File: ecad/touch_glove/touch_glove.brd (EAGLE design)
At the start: 70.4 x 40.6 mm, 181 parts, among them Q1 MCH3474 4A/30V/50mΩ, Q2 MCH3474 4A/30V/50mΩ, Q3 MCH3474 4A/30V/50mΩ, Q4 MCH3474 4A/30V/50mΩ, Q5 MCH3474 4A/30V/50mΩ, Q6 MCH3474 4A/30V/50mΩ, SW1 4A/28V, Y2 16MHz

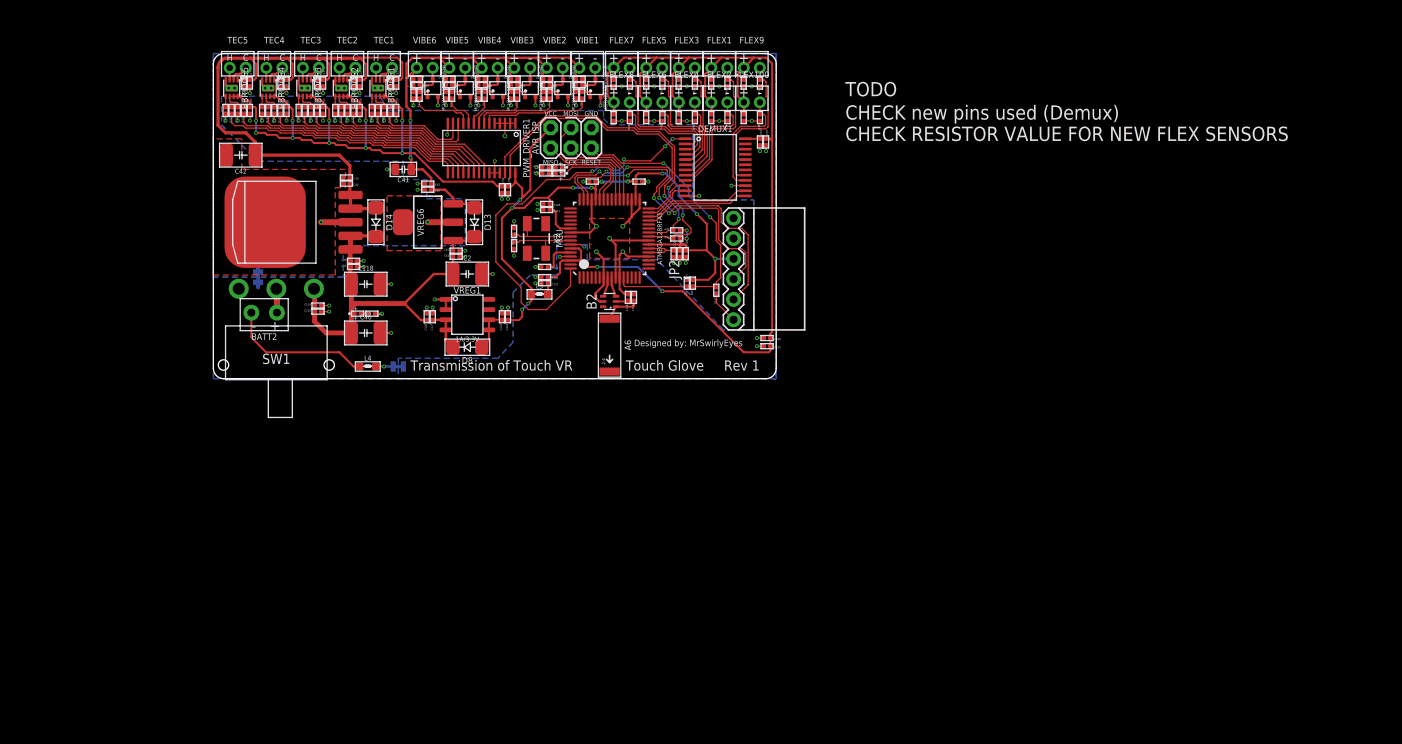
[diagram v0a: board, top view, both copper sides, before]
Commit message: Rev 2: Complete transformation.  Start by replacing parts with new 3D models and new packages.
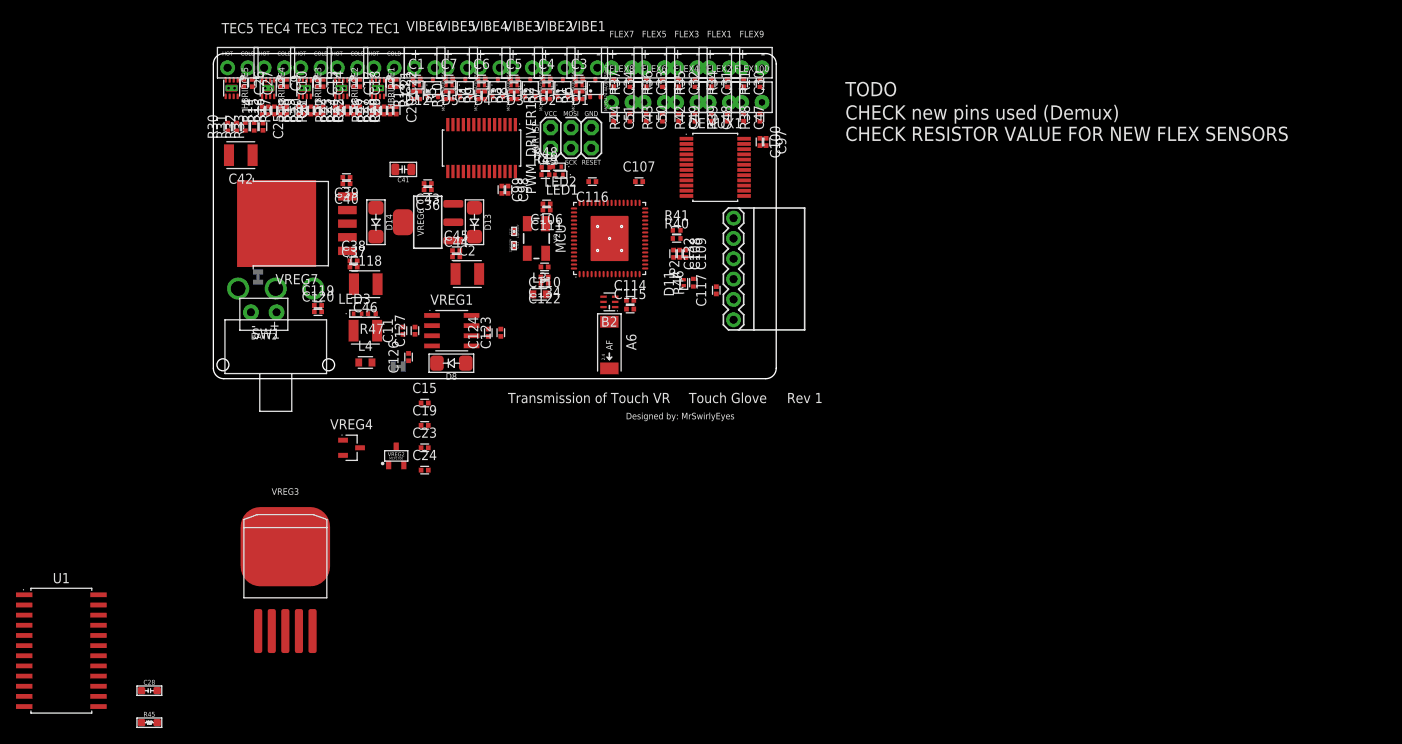
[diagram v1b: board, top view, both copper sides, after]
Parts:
- removed C135: 0.1uF/50V, PiB_capacitors:_CER_SMD_0402
- removed C136: 1uF/25V, PiB_capacitors:_CER_SMD_0402
- added C11, C15, C23: 0.1uF/50V, PiB_capacitors:CAPC1005X55
- added C19, C24: 10uF/6.3V, PiB_capacitors:CAPC1005X55
- added C28: 0.1uF/25V, PiB_capacitors:_CER_SMD-603
- added R45: 1KΩ, PiB_resistors:RESISTOR_SMD-603
- added U1: (no value), PiB:SOIC127P1030X265-24
- added VREG2: 3.3V/250mA, PiB_ic_power:MCP1700_SOT-23
- added VREG3: 5A/5V, PiB_ic_power:TO-263-5
- added VREG4: (no value), PiB_ic_power:SOT95P237X112-3
- A6: value 2.4GHz/802.11/0.5dBi/3W -> 2.45GHz; device PiB_radio_frequency:ANTENNA-CHIP5 -> PiB_radio_frequency:ANTC6522X100
- B2: value Impedence UNBAL/BAL (50Ω/100Ω) -> 50/100; device PiB_radio_frequency:0805_BALUN -> PiB_radio_frequency:RESCAXE65P200X125X95-6
- C1, C100, C106, C107, C108, C109, C110, C111, C115, C116, C117, C119, C12, C122, C124, C127, C13, C132, C134, C16, C17, C20, C21, C25, C26, C3, C30, C31, C32, C33, C34, C36, C38, C4, C40, C45, C47, C48, C49, C5, C50, C51, C6, C7, C8, C9, C98: device PiB_capacitors:_CER_SMD_0402 -> PiB_capacitors:CAPC1005X55
- C10, C120, C123, C126, C14, C18, C22, C27, C37, C39, C43, C44, C97, C99: value 10uF/10V -> 10uF/6.3V; device PiB_capacitors:_CER_SMD_0402 -> PiB_capacitors:CAPC1005X55
- C112, C113: device PiB_capacitors:_CER_SMD_0402 -> PiB_capacitors:_CER_SMD-402
- C114: value 22pF/50V -> 22pF/100V; device PiB_capacitors:_CER_SMD_0402 -> PiB_capacitors:CAPC1005X55
- C118, C2, C42, C46: device PiB_capacitors:_CER_SMD-1210 -> PiB_capacitors:CAPC3225X270
- D1, D11, D12, D2, D3, D4, D5: device PiB_discrete_semiconductors:SOD-923F/0402 -> PiB_discrete_semiconductors:DFN100X60X55-2
- DEMUX1: device PiB:SSOP-24 -> PiB:SOP65P780X200-24
- JP2: value FTDIPTH-RA -> (none)
- L3, L4: value 10uH/0.38A -> 10uH/380mA; device PiB_inductors:_SMD-0603 -> PiB_inductors:INDC1608X60
- LED1, LED2, LED3: device PiB_leds:LED_SMD-0402 -> PiB_leds:LEDC1005X40
- MCU: value ATMEGA128RFA1 -> ATMEGA128RFA1_VFQFN-64_NO-EXPOSED-PAD; device PiB_ic_microcontrollers:VFQFN-64 -> PiB_ic_microcontrollers:QFN50P900X900X90-64
- PWM_DRIVER1: device PiB:TSSOP-28 -> PiB:SOP65P650X110-28
- R1, R12, R14, R16, R18, R2, R20, R22, R24, R26, R28, R3, R30, R32, R4, R46, R47, R5: device PiB_resistors:RESISTOR_SMD-0402 -> PiB_resistors:RESC1005X35
- R10, R13, R15, R17, R19, R21, R23, R25, R27, R29, R31, R33, R6, R7, R8, R9: value 100Ω -> 100; device PiB_resistors:RESISTOR_SMD-0402 -> PiB_resistors:RESC1005X35
- R11, R34, R35, R36, R37, R38, R39, R42, R43, R44: value 47KΩ -> 47K; device PiB_resistors:RESISTOR_SMD-0402 -> PiB_resistors:RESC1005X35
- R40, R41: value 4.7KΩ -> 4.7K; device PiB_resistors:RESISTOR_SMD-0402 -> PiB_resistors:RESC1005X35
- R48: value 2KΩ -> 2K; device PiB_resistors:RESISTOR_SMD-0402 -> PiB_resistors:RESC1005X35
- R49: value 1KΩ -> 1K; device PiB_resistors:RESISTOR_SMD-0402 -> PiB_resistors:RESC1005X35
- SW1: device PiB_switches:SW_SLIDE_RA_SPDT_4A-28V_L12.7-W9.5 -> PiB_switches:SW_SLIDE_SPDT_RA_PTH_12.7L-9.5W
- VREG1: device PiB_ic_power:SOIC-8_W3.9MM -> PiB_ic_power:SOIC127P600X265-8
- VREG7: device PiB_ic_power:DDPAK-5 -> PiB_ic_power:TO170P1363X457-6
- moved C126 5.53 mm to (24.4, 2.70)
- moved C127 2.83 mm to (25.2, 6.00)
- moved D8 2.83 mm to (29.8, 1.94)
- moved VREG1 2.79 mm to (29.8, 6.00)
- moved C124 2.62 mm to (34.4, 5.75)
- moved C25 2.60 mm to (6.20, 31.5)
- moved SW1 2.48 mm to (7.80, 4.00), turned to 0 degrees
- moved R33 2.40 mm to (5.10, 31.5)
- moved R32 2.24 mm to (4.00, 31.5)
- moved C123 2.19 mm to (35.9, 5.75)
- moved R31 2.12 mm to (2.90, 31.5)
- moved VREG7 2.07 mm to (10.4, 19.4), turned to 180 degrees
- moved R30 2.05 mm to (1.80, 31.5)
- moved C115 1.54 mm to (52.1, 8.70), turned to 0 degrees
- moved L4 0.58 mm to (19.0, 2.02)
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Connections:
- new net N$33: C15.1, C19.1, L3.2, VREG4.3
- new net N$34: R45.2, U1.17
- net AGND: now also C23.2, C24.2, MCU.EP; no longer C135.2, C136.2
- net AVCC: now also C23.1, C24.1, VREG4.2; no longer C135.1, C136.1, L3.2, MCU.62
- net BATT_+: now also SW1.S1, U1.11; no longer SW1.P
- net GND: now also C112.P$2, C113.P$2, C15.2, C19.2, VREG4.1; no longer C112.2, C113.2
- net N$44: now also C113.P$1; no longer C113.1
- net N$48: now also C112.P$1; no longer C112.1
- net N$49: now also A6.1; no longer A6.FEED
- net NGND: no longer VREG7.TAB
- net VBATT: now also SW1.P; no longer SW1.S1
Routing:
- net VCC: track 180.6 -> 0.00 mm, vias 23 -> 0
- net AVCC: track 146.1 -> 0.00 mm, vias 2 -> 0
- net GND: track 107.5 -> 0.00 mm, vias 52 -> 0
- net 1.8V: track 85.0 -> 0.00 mm
- net 3.3V: track 70.5 -> 0.00 mm, vias 2 -> 0
- net VBATT: track 57.4 -> 0.00 mm
- net A1: track 50.7 -> 0.00 mm, vias 4 -> 0
- net SCL: track 45.0 -> 0.00 mm, vias 2 -> 0
- net TX0: track 44.0 -> 0.00 mm, vias 4 -> 0
- net RESET: track 41.1 -> 0.00 mm, vias 2 -> 0
- net SDA: track 40.8 -> 0.00 mm, vias 2 -> 0
- net NGND: track 40.4 -> 0.00 mm, vias 27 -> 0
- net RX0: track 39.9 -> 0.00 mm, vias 4 -> 0
- net AGND: track 31.4 -> 0.00 mm, vias 20 -> 0
- net TEC_5_COLD: track 31.4 -> 0.00 mm
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- added copper zone on layer 15, net GND
- added copper zone on layer 2, net VCC
- removed copper zone on layer 16, net AGND
- removed copper zone on layer 1, net GND
- removed copper zone on layer 16, net GND
- removed copper zone on layer 1, net NGND
- removed copper zone on layer 16, net NGND

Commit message: Several more replacements and moved parts such that they are snapped to the grid.
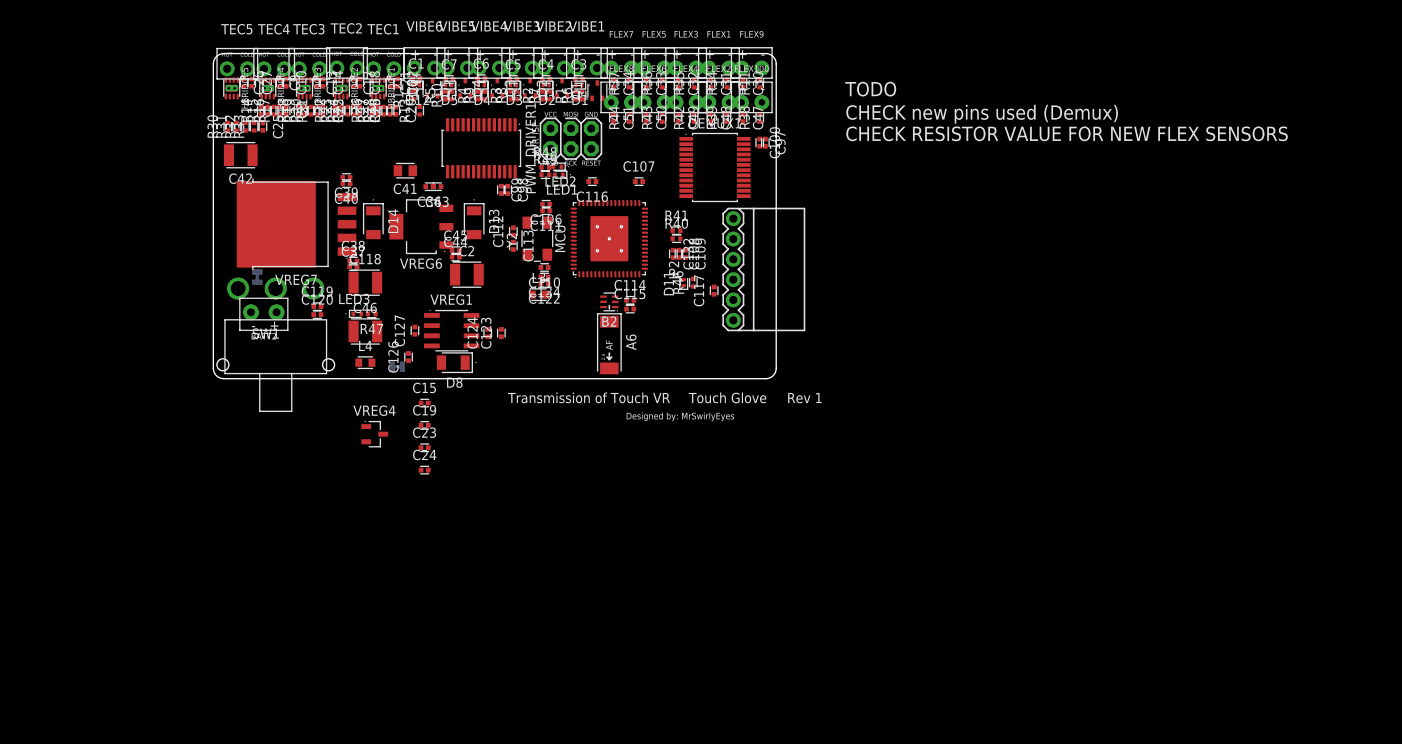
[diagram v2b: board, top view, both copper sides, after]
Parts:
- removed C11: 0.1uF/50V, PiB_capacitors:CAPC1005X55
- removed C28: 0.1uF/25V, PiB_capacitors:_CER_SMD-603
- removed R45: 1KΩ, PiB_resistors:RESISTOR_SMD-603
- removed U1: (no value), PiB:SOIC127P1030X265-24
- removed VREG2: 3.3V/250mA, PiB_ic_power:MCP1700_SOT-23
- removed VREG3: 5A/5V, PiB_ic_power:TO-263-5
- C1, C10, C100, C106, C107, C108, C109, C110, C111, C114, C115, C116, C117, C119, C12, C120, C122, C123, C124, C126, C127, C13, C132, C134, C14, C15, C16, C17, C18, C19, C20, C21, C22, C23, C24, C25, C26, C27, C3, C30, C31, C32, C33, C34, C36, C37, C38, C39, C4, C40, C43, C44, C45, C47, C48, C49, C5, C50, C51, C6, C7, C8, C9, C97, C98, C99: device PiB_capacitors:CAPC1005X55 -> PiB_capacitors:CAPC1005X55_SMD-0402
- C112, C113: device PiB_capacitors:_CER_SMD-402 -> PiB_capacitors:CAPC1005X55_SMD-0402
- C118, C2, C42, C46: device PiB_capacitors:CAPC3225X270 -> PiB_capacitors:CAPC3225X270_SMD-1210
- C41: value 47uF/10V -> 47uF/6.3V; device PiB_capacitors:_CER_SMD-805 -> PiB_capacitors:CAPC2012X95_SMD-0805
- D13, D14, D8: device PiB_discrete_semiconductors:SOD123F -> PiB_discrete_semiconductors:SODFL3516X170
- Q1, Q2, Q3, Q4, Q5, Q6: value MCH3474 4A/30V/50mΩ -> MCH3474 4A/30V; device PiB_discrete_semiconductors:SC-70FL/MCPH3 -> PiB_discrete_semiconductors:SOTFL65P209X90-3
- VREG4: value (none) -> 250mA/3.3V; device PiB_ic_power:SOT95P237X112-3 -> PiB_ic_power:SOT95P237X112-3_SOT-23-3
- VREG6: device PiB_ic_power:SOT223-4 -> PiB_ic_power:SOT229P700X180-4
- Y2: value 16MHz -> 16 MHz; device PiB:CRYSTAL-SMD-5X3 -> PiB:OSCCC500X320X110
- moved VREG4 3.36 mm to (20.2, -6.94)
- moved R13 1.93 mm to (25.8, 33.5)
- moved C43 1.26 mm to (28.0, 24.0)
- moved VREG6 0.97 mm to (26.0, 19.0), turned to 180 degrees
- moved C36 0.43 mm to (27.0, 24.0)
- moved Q1 0.41 mm to (48.0, 36.0), turned to 90 degrees
- moved C120 0.39 mm to (13.0, 8.00)
- moved D14 0.33 mm to (20.0, 19.5)
- moved C41 0.30 mm to (24.0, 26.0)
- moved C117 0.27 mm to (62.6, 11.0)
- moved D8 0.26 mm to (30.0, 2.00)
- moved TEC3 0.23 mm to (12.0, 40.0)
- moved C118 0.20 mm to (19.0, 12.0)
- moved C119 0.17 mm to (13.0, 9.00)
- moved C22 0.15 mm to (23.0, 37.0)
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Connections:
- removed net N$34: R45.2, U1.17
- removed net N$44: C113.P$1, MCU.57, Y2.3
- removed net N$48: C112.P$1, MCU.56, Y2.1
- new net N$35: C112.1, MCU.56, Y2.3
- new net N$36: C113.1, MCU.57, Y2.1
- net BATT_+: no longer U1.11
- net GND: now also C112.2, C113.2; no longer C112.P$2, C113.P$2
- net N$15: now also Q2.2; no longer Q2.3
- net N$17: now also Q1.2; no longer Q1.3
- net N$2: now also Q4.2; no longer Q4.3
- net N$3: now also Q5.2; no longer Q5.3
- net N$30: now also Q6.2; no longer Q6.3
- net N$4: now also Q3.2; no longer Q3.3
- net NGND: now also Q1.3, Q2.3, Q3.3, Q4.3, Q5.3, Q6.3, VREG6.4; no longer Q1.2, Q2.2, Q3.2, Q4.2, Q5.2, Q6.2, VREG6.TAB

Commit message: Start and complete much of the 4 layer routing.  All components on board have 3D models.
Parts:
- removed ANALOG_BR: 2PT_GND_TIE, PiB_power_symbols:2PT_GND_TIE
- removed BATT2: BATTERYPTH_HOLES, PiB:DUAL_PTH_PADS
- removed C1, C3, C4, C5, C6, C7: 0.1uF/50V, PiB_capacitors:CAPC1005X55_SMD-0402
- removed C10, C14, C18, C22, C27: 10uF/6.3V, PiB_capacitors:CAPC1005X55_SMD-0402
- added LIPO1: Molex RA 2mm pitch, PiB_batteries:BATTERY_MOLEX-89401_RA_PITCH-2MM
- added U$1: (no value), PiB_logo:MRSWIRLYEYES-LOGO
- AVR_ISP: value AVR ISP -> AVRISP
- FLEX1, FLEX3, FLEX5, FLEX7, FLEX9: device PiB:CONNECTOR_FSR -> PiB_sensors:_MOLEX-0530480210_RA_PITCH-1.25MM
- FLEX100, FLEX2, FLEX4, FLEX6, FLEX8: device PiB:CONNECTOR_FSR -> PiB_sensors:_MOLEX-0530470210_VERT_PITCH-1.25MM
- HBRIDGE1, HBRIDGE2, HBRIDGE3, HBRIDGE4, HBRIDGE5: value DRV8837C -> DRV8837C 1A
- JP2: value (none) -> FTDI
- TEC1, TEC2, TEC3, TEC4, TEC5: value PELTIER -> Molex RA 1.25mm pitch; device PiB:CONNECTOR_PELTIER -> PiB_actuators:_MOLEX-0530480210_RA_PITCH-1.25MM
- VIBE1, VIBE2, VIBE3, VIBE4, VIBE5, VIBE6: value VIBE_MOTOR -> Molex RA 1.25mm pitch; device PiB:CONNECTOR_VIBE-MOTOR -> PiB_actuators:_MOLEX-0530480210_RA_PITCH-1.25MM
- moved C24 32.8 mm to (50.2, 11.2), turned to 90 degrees
- moved VREG4 32.6 mm to (46.9, 11.8), turned to 90 degrees
- moved C23 30.1 mm to (49.1, 11.2), turned to 90 degrees
- moved L4 28.4 mm to (46.7, 8.40)
- moved AVR_ISP 27.5 mm to (71.8, 25.3)
- moved C19 25.1 mm to (43.6, 12.4), turned to 270 degrees
- moved R49 24.9 mm to (66.3, 27.5), turned to 180 degrees
- moved R48 24.8 mm to (66.3, 26.4), turned to 180 degrees
- moved C97 24.3 mm to (48.5, 16.4), turned to 180 degrees
- moved R31 24.3 mm to (25.6, 22.9), turned to 180 degrees
- moved C15 23.9 mm to (44.7, 12.4), turned to 270 degrees
- moved C100 23.2 mm to (48.5, 17.5), turned to 180 degrees
- moved R33 21.8 mm to (25.6, 24.0), turned to 180 degrees
- moved LED2 21.2 mm to (64.2, 26.4), turned to 0 degrees
- moved LED1 21.1 mm to (64.2, 27.5), turned to 0 degrees
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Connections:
- removed net BATT_+: BATT2.+, SW1.S1
- removed net C10: DEMUX1.21
- removed net C11: DEMUX1.20
- removed net C12: DEMUX1.19
- removed net C13: DEMUX1.18
- removed net C8: DEMUX1.23
- removed net C9: DEMUX1.22
- removed net N$52: ANALOG_BR.P$1, L4.2
- new net +: LIPO1.+, SW1.S1
- net 1.8V: no longer C10.1, C14.1, C18.1, C22.1, C27.1
- net 3.3V: no longer C1.1, C3.1, C4.1, C5.1, C6.1, C7.1
- net A0: now also DEMUX1.1
- net A1: no longer DEMUX1.1
- net AGND: now also B2.5, C110.2, C114.2, C115.2, DEMUX1.16, DEMUX1.17, DEMUX1.18, DEMUX1.19, DEMUX1.20, DEMUX1.21, L4.2, MCU.10, MCU.7, MCU.P$1, MCU.P$2, MCU.P$3, MCU.P$4, MCU.P$5; no longer ANALOG_BR.P$2
- net AVCC: now also FLEX1.1, FLEX100.1, FLEX2.1, FLEX3.1, FLEX4.1, FLEX5.1, FLEX6.1, FLEX7.1, FLEX8.1, FLEX9.1; no longer FLEX1.+, FLEX100.+, FLEX2.+, FLEX3.+, FLEX4.+, FLEX5.+, FLEX6.+, FLEX7.+, FLEX8.+, FLEX9.+
- net GND: now also AVR_ISP.GND, LIPO1.-, R1.1, R12.1, R2.1, R3.1, R4.1, R5.1; no longer AVR_ISP.6, B2.5, BATT2.-, C110.2, C114.2, C115.2, MCU.10, MCU.7
- net MISO: now also AVR_ISP.MISO; no longer AVR_ISP.1
- net MOSI: now also AVR_ISP.MOSI; no longer AVR_ISP.4
- net N$1: now also TEC5.1; no longer TEC5.HOT
- net N$11: now also TEC4.1; no longer TEC4.HOT
- net N$12: now also TEC3.1; no longer TEC3.HOT
- net N$15: no longer C4.2
- net N$16: now also TEC3.2; no longer TEC3.COLD
- net N$17: no longer C3.2
- net N$18: now also TEC2.1; no longer TEC2.HOT
- net N$2: no longer C6.2
- net N$23: now also TEC2.2; no longer TEC2.COLD
- net N$24: now also TEC1.1; no longer TEC1.HOT
- net N$27: now also TEC1.2; no longer TEC1.COLD
- net N$3: no longer C7.2
- net N$30: no longer C1.2
- net N$4: no longer C5.2
- net N$5: now also TEC5.2; no longer TEC5.COLD
- net N$6: now also TEC4.2; no longer TEC4.COLD
- net NGND: now also VREG7.6; no longer C10.2, C14.2, C18.2, C22.2, C27.2, R1.1, R12.1, R2.1, R3.1, R4.1, R5.1
- net PD4: now also DEMUX1.10; no longer DEMUX1.13
- net PD5: now also DEMUX1.11; no longer DEMUX1.14
- net PD6: now also DEMUX1.13; no longer DEMUX1.11
- net PD7: now also DEMUX1.14; no longer DEMUX1.10
- net RESET: now also AVR_ISP.RESET; no longer AVR_ISP.5
- net SCK: now also AVR_ISP.SCK; no longer AVR_ISP.3
- net STRAIN_1: now also DEMUX1.5, FLEX1.2; no longer DEMUX1.9, FLEX1.-
- net STRAIN_10: now also DEMUX1.23, FLEX100.2; no longer DEMUX1.16, FLEX100.-
- net STRAIN_2: now also DEMUX1.22, FLEX2.2; no longer DEMUX1.8, FLEX2.-
- net STRAIN_3: now also DEMUX1.4, FLEX3.2; no longer DEMUX1.7, FLEX3.-
- net STRAIN_4: now also DEMUX1.9, FLEX4.2; no longer DEMUX1.6, FLEX4.-
- net STRAIN_5: now also DEMUX1.3, FLEX5.2; no longer DEMUX1.5, FLEX5.-
- net STRAIN_6: now also DEMUX1.8, FLEX6.2; no longer DEMUX1.4, FLEX6.-
- net STRAIN_7: now also DEMUX1.2, FLEX7.2; no longer DEMUX1.3, FLEX7.-
- net STRAIN_8: now also DEMUX1.7, FLEX8.2; no longer DEMUX1.2, FLEX8.-
- net STRAIN_9: now also DEMUX1.6, FLEX9.2; no longer DEMUX1.17, FLEX9.-
- net TEC_1_COLD: now also PWM_DRIVER1.13; no longer PWM_DRIVER1.12
- net TEC_1_HOT: now also PWM_DRIVER1.12; no longer PWM_DRIVER1.13
- net VCC: no longer AVR_ISP.2, JP2.VCC
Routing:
- net GND: track 0.00 -> 57.7 mm, vias 0 -> 56
- net VCC: track 0.00 -> 49.6 mm, vias 0 -> 16
- net AGND: track 0.00 -> 48.8 mm, vias 0 -> 49
- net SCL: track 0.00 -> 45.1 mm, vias 0 -> 2
- net A0: track 0.00 -> 43.6 mm
- net STRAIN_9: track 0.00 -> 39.4 mm
- net SDA: track 0.00 -> 39.4 mm, vias 0 -> 2
- net PD6: track 0.00 -> 35.5 mm, vias 0 -> 2
- net PD4: track 0.00 -> 34.5 mm, vias 0 -> 2
- net STRAIN_10: track 0.00 -> 34.0 mm
- net PD5: track 0.00 -> 33.9 mm, vias 0 -> 2
- net STRAIN_1: track 0.00 -> 33.9 mm
- net PD7: track 0.00 -> 33.1 mm, vias 0 -> 2
- net AVCC: track 0.00 -> 31.2 mm, vias 0 -> 3
- net N$29: track 0.00 -> 30.0 mm
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- added copper zone on layer 1, net AGND
- added copper zone on layer 15, net AGND
- added copper zone on layer 2, net AGND
- added copper zone on layer 2, net AVCC
- added copper zone on layer 15, net N$34
- added copper zone on layer 2, net N$34
- added copper zone on layer 15, net NGND
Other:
- board size 70.4 x 40.6 mm -> 78.3 x 40.6 mm
- board text added: "Touch Glove Rev 2"
- board text removed: "Touch Glove Rev 1"
